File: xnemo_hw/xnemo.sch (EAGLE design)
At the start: 49 parts, among them J1 MICRO_USB_B_RECEPT, J2 DM3D_MICRO_SD, J3 HEADER_2X5_0.05_SMD, J4 HEADER_2X7, U1 LTC3559, U10 STTS751, U2 L3GD20, U4 STM32F407VE, U7 LSM303DLHC, U8 LSM303DLHC, U9 L3GD20, X1 TXC_7A_XTAL

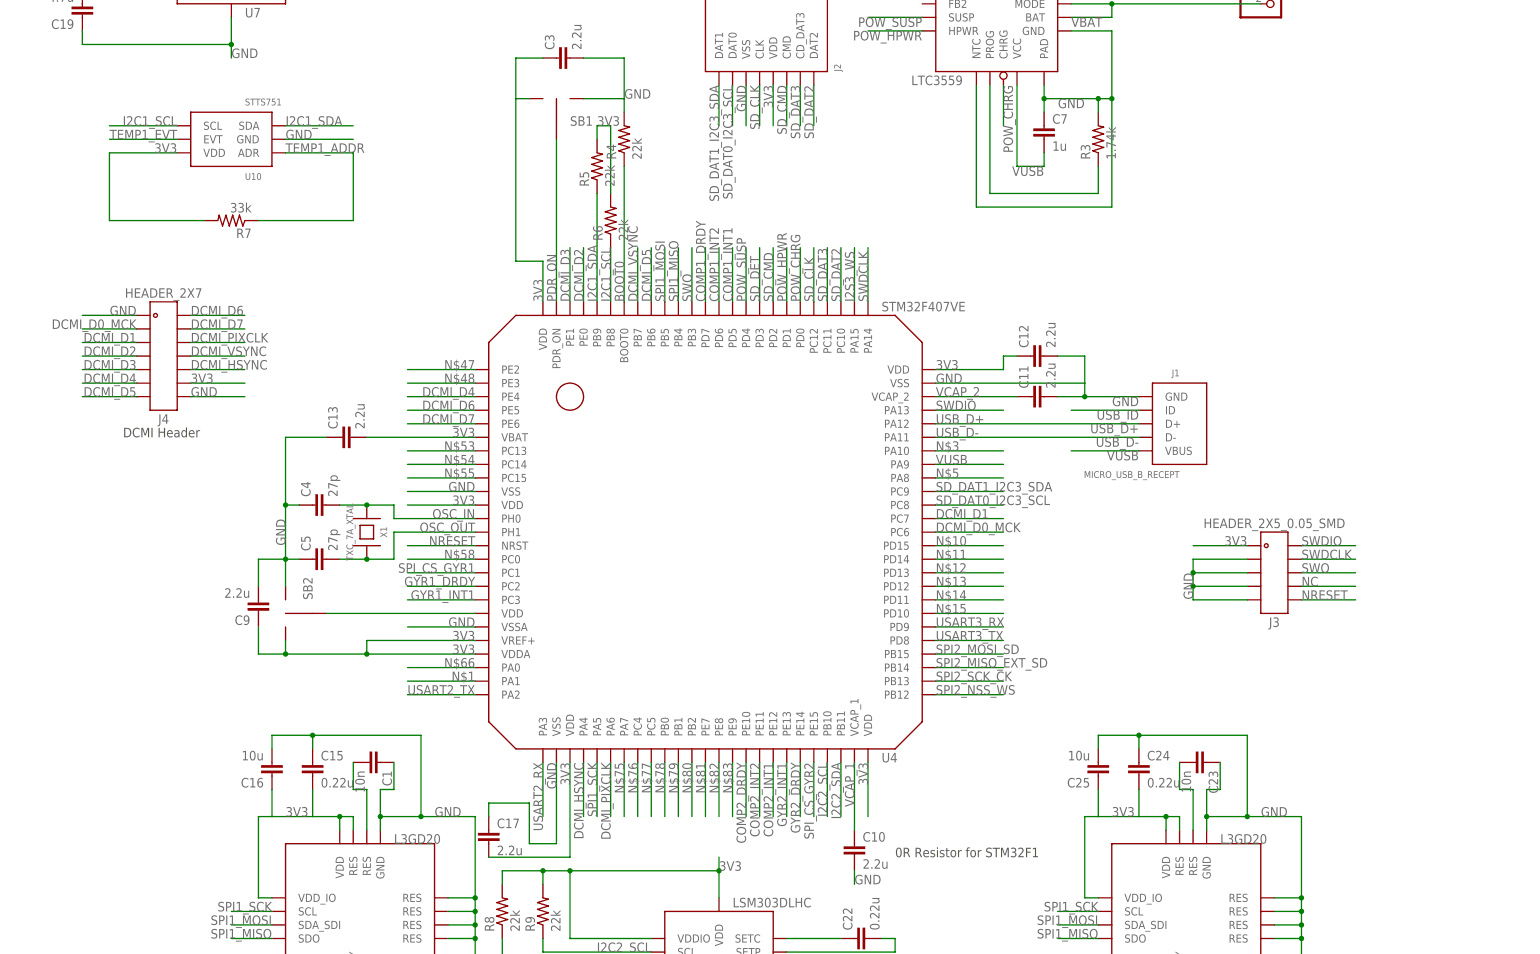
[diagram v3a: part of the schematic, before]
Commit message: Added datasheet, fixed some footprints
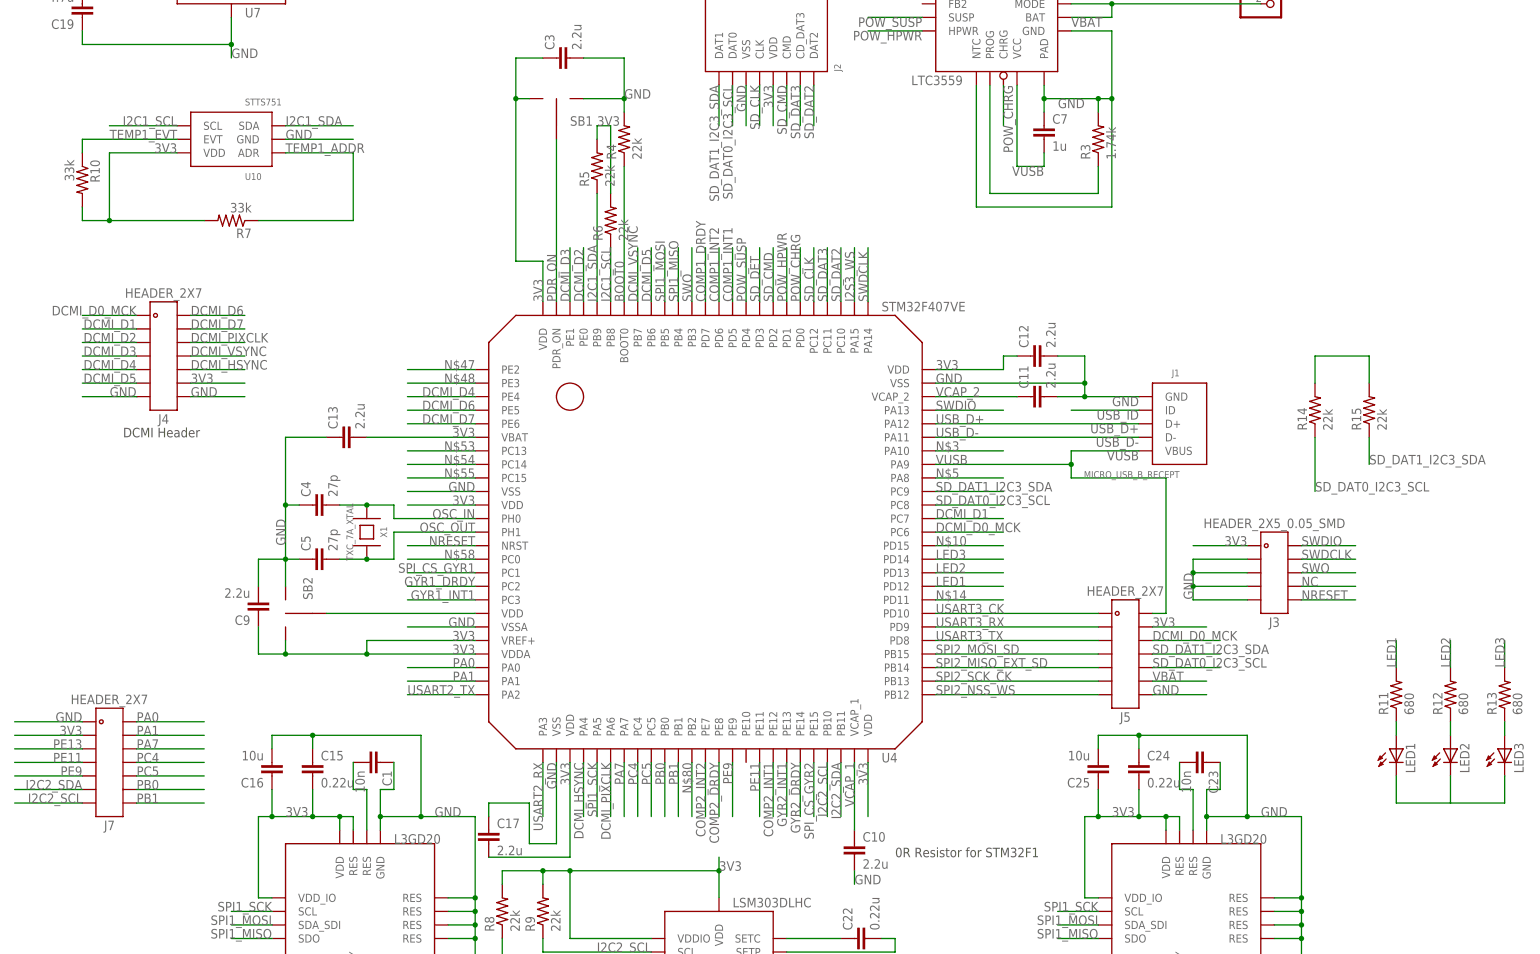
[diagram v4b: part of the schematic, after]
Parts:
- added J5, J7: HEADER_2X7, xnemo:HEADER_2X7
- added LED1, LED2, LED3: (no value), led:LEDSML0805
- added R10: 33k, resistor:R-US_R0402
- added R11, R12, R13: 680, resistor:R-US_R0402
- added R14, R15: 22k, resistor:R-US_R0402
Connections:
- removed net N$1: U4.PA1
- removed net N$11: U4.PD14
- removed net N$12: U4.PD13
- removed net N$13: U4.PD12
- removed net N$15: U4.PD10
- removed net N$66: U4.PA0
- removed net N$75: U4.PA7
- removed net N$76: U4.PC4
- removed net N$77: U4.PC5
- removed net N$78: U4.PB0
- removed net N$79: U4.PB1
- removed net N$81: U4.PE7
- removed net N$82: U4.PE8
- removed net N$83: U4.PE9
- new net LED1: R11.2, U4.PD12
- new net LED2: R12.2, U4.PD13
- new net LED3: R13.2, U4.PD14
- new net N$16: LED2.A, R12.1
- new net N$17: LED3.A, R13.1
- new net N$8: LED1.C, LED2.C, LED3.C
- new net N$9: LED1.A, R11.1
- new net PA0: J7.2, U4.PA0
- new net PA1: J7.4, U4.PA1
- new net PA7: J7.6, U4.PA7
- new net PB0: J7.12, U4.PB0
- new net PB1: J7.14, U4.PB1
- new net PC4: J7.8, U4.PC4
- new net PC5: J7.10, U4.PC5
- new net PE11: J7.7, U4.PE11
- new net PE13: J7.5
- new net PE9: J7.9, U4.PE9
- new net USART3_CK: J5.1, U4.PD10
- net 3V3: now also J4.12, J5.4, J7.3, R10.2, R14.2, R15.2; no longer J4.11
- net COMP2_DRDY: now also U4.PE8; no longer U4.PE10
- net COMP2_INT2: now also U4.PE7; no longer U4.PE11
- net DCMI_D0_MCK: now also J4.1, J5.6; no longer J4.4
- net DCMI_D1: now also J4.3; no longer J4.6
- net DCMI_D2: now also J4.5; no longer J4.8
- net DCMI_D3: now also J4.7; no longer J4.10
- net DCMI_D4: now also J4.9; no longer J4.12
- net DCMI_D5: now also J4.11; no longer J4.14
- net DCMI_D6: now also J4.2; no longer J4.1
- net DCMI_D7: now also J4.4; no longer J4.3
- net DCMI_HSYNC: now also J4.10; no longer J4.9
- net DCMI_PIXCLK: now also J4.6; no longer J4.5
- net DCMI_VSYNC: now also J4.8; no longer J4.7
- net GND: now also J4.14, J5.14, J7.1; no longer J4.2
- net I2C2_SCL: now also J7.13
- net I2C2_SDA: now also J7.11
- net SD_DAT0_I2C3_SCL: now also J5.10, R14.1
- net SD_DAT1_I2C3_SDA: now also J5.8, R15.1
- net SPI2_MISO_EXT_SD: now also J5.9
- net SPI2_MOSI_SD: now also J5.7
- net SPI2_NSS_WS: now also J5.13
- net SPI2_SCK_CK: now also J5.11
- net TEMP1_EVT: now also R10.1
- net USART3_RX: now also J5.3
- net USART3_TX: now also J5.5
- net VBAT: now also J5.12
- net VUSB: now also J5.2

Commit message: All connections made -- no DRC yet
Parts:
- J7: value HEADER_2X7 -> HEADER_2X8; device xnemo:HEADER_2X7 -> xnemo:HEADER_2X8
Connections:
- removed net I2S3_WS: U4.PA15
- removed net N$8: LED1.C, LED2.C, LED3.C
- net GND: now also LED1.C, LED2.C, LED3.C
- net USART2_RX: now also J7.16
- net USART2_TX: now also J7.15
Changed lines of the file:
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@@
 <class number="0" name="default" width="0" drill="0">
+</class>
+<class number="1" name="power" width="0" drill="0">
 </class>
 </classes>
@@
 <part name="R14" library="resistor" deviceset="R-US_" device="R0402" value="22k"/>
 <part name="R15" library="resistor" deviceset="R-US_" device="R0402" value="22k"/>
-<part name="J7" library="xnemo" deviceset="HEADER_2X7" device=""/>
+<part name="J7" library="xnemo" deviceset="HEADER_2X8" device=""/>
 </parts>
 <sheets>
@@
 </busses>
 <nets>
-<net name="3V3" class="0">
+<net name="3V3" class="1">
 <segment>
 <wire x1="-190.5" y1="-129.54" x2="-190.5" y2="-127" width="0.1524" layer="91"/>
@@
 <wire x1="-53.34" y1="53.34" x2="-60.96" y2="53.34" width="0.1524" layer="91"/>
 <wire x1="-60.96" y1="53.34" x2="-60.96" y2="55.88" width="0.1524" layer="91"/>
+<junction x="-53.34" y="53.34"/>
 </segment>
 <segment>
@@
 <pinref part="R15" gate="G$1" pin="2"/>
 <wire x1="0" y1="-40.64" x2="0" y2="-45.72" width="0.1524" layer="91"/>
+<label x="-7.62" y="-40.64" size="1.778" layer="95"/>
 </segment>
 <segment>
@@
 <pinref part="C2" gate="G$1" pin="2"/>
 <wire x1="-60.96" y1="63.5" x2="-60.96" y2="66.04" width="0.1524" layer="91"/>
+<junction x="-60.96" y="66.04"/>
 </segment>
 <segment>
@@
 <label x="-241.3" y="-109.22" size="1.778" layer="95" rot="MR0"/>
 </segment>
+<segment>
+<pinref part="LED1" gate="G$1" pin="C"/>
+<wire x1="5.08" y1="-119.38" x2="5.08" y2="-124.46" width="0.1524" layer="91"/>
+<pinref part="LED3" gate="G$1" pin="C"/>
+<wire x1="5.08" y1="-124.46" x2="15.24" y2="-124.46" width="0.1524" layer="91"/>
+<wire x1="15.24" y1="-124.46" x2="25.4" y2="-124.46" width="0.1524" layer="91"/>
+<wire x1="25.4" y1="-124.46" x2="25.4" y2="-119.38" width="0.1524" layer="91"/>
+<pinref part="LED2" gate="G$1" pin="C"/>
+<wire x1="15.24" y1="-119.38" x2="15.24" y2="-124.46" width="0.1524" layer="91"/>
+<junction x="15.24" y="-124.46"/>
+</segment>
 </net>
 <net name="GYR_RES1" class="0">
@@
 </segment>
 </net>
-<net name="I2S3_WS" class="0">
-<segment>
-<pinref part="U4" gate="G$1" pin="PA15"/>
-<wire x1="-96.52" y1="-30.48" x2="-96.52" y2="-20.32" width="0.1524" layer="91"/>
-<label x="-96.52" y="-30.48" size="1.778" layer="95" rot="R90"/>
-</segment>
-</net>
 <net name="SPI1_MISO" class="0">
 <segment>
@@
 <label x="-167.64" y="-104.14" size="1.778" layer="95" rot="MR0"/>
 </segment>
+<segment>
+<pinref part="J7" gate="G$1" pin="15"/>
+<wire x1="-241.3" y1="-127" x2="-254" y2="-127" width="0.1524" layer="91"/>
+<label x="-241.3" y="-127" size="1.778" layer="95" rot="MR0"/>
+</segment>
 </net>
 <net name="USART2_RX" class="0">
@@
 <wire x1="-154.94" y1="-116.84" x2="-154.94" y2="-127" width="0.1524" layer="91"/>
 <label x="-154.94" y="-116.84" size="1.778" layer="95" rot="MR270"/>
+</segment>
+<segment>
+<pinref part="J7" gate="G$1" pin="16"/>
+<wire x1="-231.14" y1="-127" x2="-218.44" y2="-127" width="0.1524" layer="91"/>
+<label x="-231.14" y="-127" size="1.778" layer="95"/>
 </segment>
 </net>
@@
 </segment>
 </net>
-<net name="N$8" class="0">
-<segment>
-<pinref part="LED1" gate="G$1" pin="C"/>
-<wire x1="5.08" y1="-119.38" x2="5.08" y2="-124.46" width="0.1524" layer="91"/>
-<pinref part="LED3" gate="G$1" pin="C"/>
-<wire x1="5.08" y1="-124.46" x2="15.24" y2="-124.46" width="0.1524" layer="91"/>
-<wire x1="15.24" y1="-124.46" x2="25.4" y2="-124.46" width="0.1524" layer="91"/>
-<wire x1="25.4" y1="-124.46" x2="25.4" y2="-119.38" width="0.1524" layer="91"/>
-<pinref part="LED2" gate="G$1" pin="C"/>
-<wire x1="15.24" y1="-119.38" x2="15.24" y2="-124.46" width="0.1524" layer="91"/>
-</segment>
-</net>

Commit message: Added microphone, DRC passed, no airwires
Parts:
- added SB3: SOLDER_BRIDGE_2, xnemo:SOLDER_BRIDGE_2
- added U3: MP45DT02, xnemo:MP45DT02
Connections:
- removed net N$3: U4.PA10
- removed net N$5: U4.PA8
- new net MIC_LR: SB3.P$3, U3.LR
- new net USART1_CK: U3.CLK, U4.PA8
- new net USART1_RX: U3.DOUT, U4.PA10
- net 3V3: now also SB3.P$1, U3.VDD
- net GND: now also SB3.P$2, U3.GND@1, U3.GND@2
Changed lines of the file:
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@@
 <part name="R15" library="resistor" deviceset="R-US_" device="R0402" value="22k"/>
 <part name="J7" library="xnemo" deviceset="HEADER_2X8" device=""/>
+<part name="U3" library="xnemo" deviceset="MP45DT02" device=""/>
+<part name="SB3" library="xnemo" deviceset="SOLDER_BRIDGE_2" device=""/>
 </parts>
 <sheets>
@@
 <instance part="R15" gate="G$1" x="0" y="-50.8" rot="R90"/>
 <instance part="J7" gate="G$1" x="-236.22" y="-119.38"/>
+<instance part="U3" gate="G$1" x="-22.86" y="-17.78"/>
+<instance part="SB3" gate="G$1" x="-55.88" y="-25.4" rot="R90"/>
 </instances>
 <busses>
@@
 <wire x1="-241.3" y1="-111.76" x2="-254" y2="-111.76" width="0.1524" layer="91"/>
 <label x="-241.3" y="-111.76" size="1.778" layer="95" rot="MR0"/>
+</segment>
+<segment>
+<pinref part="U3" gate="G$1" pin="VDD"/>
+<wire x1="-12.7" y1="-15.24" x2="5.08" y2="-15.24" width="0.1524" layer="91"/>
+<label x="-12.7" y="-15.24" size="1.778" layer="95"/>
+<pinref part="SB3" gate="G$1" pin="P$1"/>
+<wire x1="-58.42" y1="-30.48" x2="-58.42" y2="-33.02" width="0.1524" layer="91"/>
+<wire x1="-58.42" y1="-33.02" x2="5.08" y2="-33.02" width="0.1524" layer="91"/>
+<wire x1="5.08" y1="-33.02" x2="5.08" y2="-15.24" width="0.1524" layer="91"/>
 </segment>
 </net>
@@
 <junction x="15.24" y="-124.46"/>
 </segment>
+<segment>
+<pinref part="U3" gate="G$1" pin="GND@2"/>
+<wire x1="-33.02" y1="-20.32" x2="-45.72" y2="-20.32" width="0.1524" layer="91"/>
+<label x="-33.02" y="-20.32" size="1.778" layer="95" rot="MR0"/>
+</segment>
+<segment>
+<pinref part="U3" gate="G$1" pin="GND@1"/>
+<label x="-33.02" y="-15.24" size="1.778" layer="95" rot="MR0"/>
+<pinref part="SB3" gate="G$1" pin="P$2"/>
+<wire x1="-33.02" y1="-15.24" x2="-58.42" y2="-15.24" width="0.1524" layer="91"/>
+<wire x1="-58.42" y1="-15.24" x2="-58.42" y2="-20.32" width="0.1524" layer="91"/>
+</segment>
 </net>
 <net name="GYR_RES1" class="0">
@@
 </segment>
 </net>
-<net name="N$3" class="0">
+<net name="USART1_RX" class="0">
 <segment>
 <pinref part="U4" gate="G$1" pin="PA10"/>
@@
 <label x="-81.28" y="-58.42" size="1.778" layer="95"/>
 </segment>
-</net>
-<net name="N$5" class="0">
+<segment>
+<pinref part="U3" gate="G$1" pin="DOUT"/>
+<wire x1="-12.7" y1="-17.78" x2="0" y2="-17.78" width="0.1524" layer="91"/>
+<label x="-12.7" y="-17.78" size="1.778" layer="95"/>
+</segment>
+</net>
+<net name="USART1_CK" class="0">
 <segment>
 <pinref part="U4" gate="G$1" pin="PA8"/>
 <wire x1="-81.28" y1="-63.5" x2="-68.58" y2="-63.5" width="0.1524" layer="91"/>
 <label x="-81.28" y="-63.5" size="1.778" layer="95"/>
+</segment>
+<segment>
+<pinref part="U3" gate="G$1" pin="CLK"/>
+<wire x1="-12.7" y1="-20.32" x2="0" y2="-20.32" width="0.1524" layer="91"/>
+<label x="-12.7" y="-20.32" size="1.778" layer="95"/>
 </segment>
 </net>
@@
 </segment>
 </net>
+<net name="MIC_LR" class="0">
+<segment>
+<pinref part="U3" gate="G$1" pin="LR"/>
+<wire x1="-33.02" y1="-17.78" x2="-48.26" y2="-17.78" width="0.1524" layer="91"/>
+<label x="-33.02" y="-17.78" size="1.778" layer="95" rot="MR0"/>
+<wire x1="-48.26" y1="-17.78" x2="-48.26" y2="-25.4" width="0.1524" layer="91"/>
+<pinref part="SB3" gate="G$1" pin="P$3"/>
+<wire x1="-48.26" y1="-25.4" x2="-50.8" y2="-25.4" width="0.1524" layer="91"/>
+</segment>
+</net>

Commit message: Attempting to genereate CAM files
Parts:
- added C18, C26, C27: 2.2u, resistor:C-EUC0603
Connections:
- net 3V3: now also C16.2, C18.2, C26.1, C27.2, J3.1; no longer C16.1, J3.2
- net GND: now also C16.1, C18.1, C26.2, C27.1, J3.3, J3.5, J3.7, J3.9; no longer C16.2, J3.10, J3.4, J3.6, J3.8
- net NC: now also J3.8; no longer J3.7
- net NRESET: now also J3.10; no longer J3.9
- net SWDCLK: now also J3.4; no longer J3.3
- net SWDIO: now also J3.2; no longer J3.1
- net SWO: now also J3.6; no longer J3.5
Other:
- moved on the sheet: C10, C16, J3
